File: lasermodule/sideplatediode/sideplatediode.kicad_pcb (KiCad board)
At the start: 2 copper layers, 117 x 33.2 mm, 4 parts, among them J1 Conn_01x02

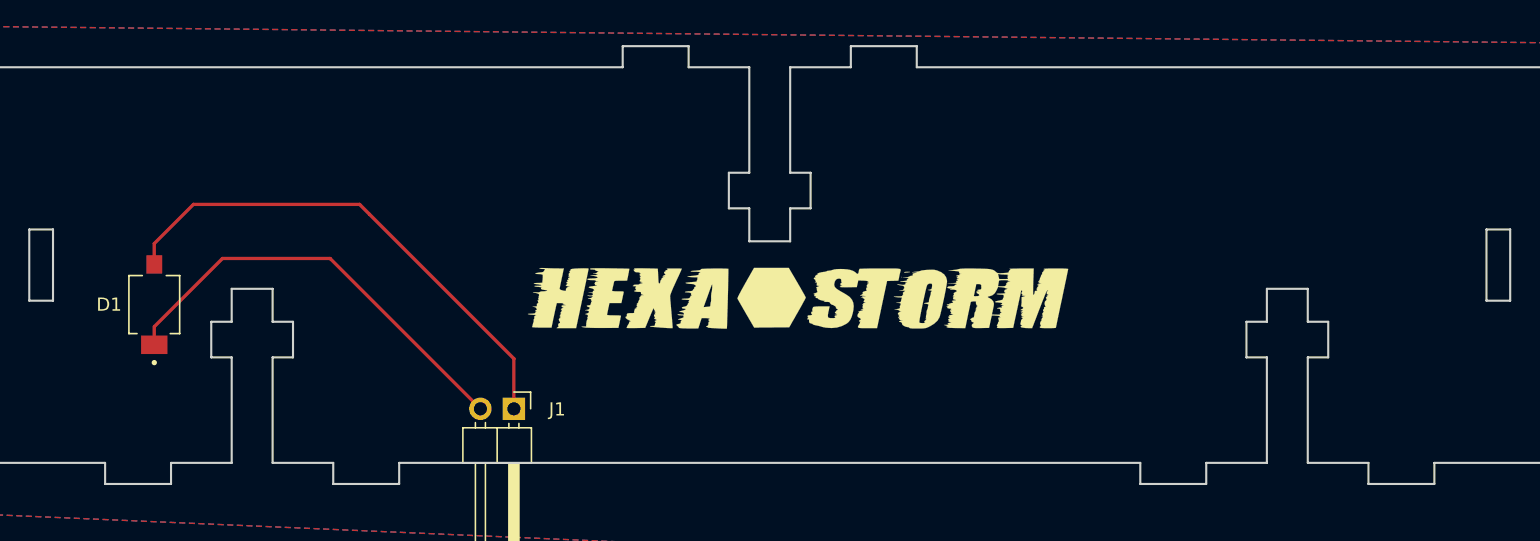
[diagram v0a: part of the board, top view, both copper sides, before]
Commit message: removed need for screws using pcb pads
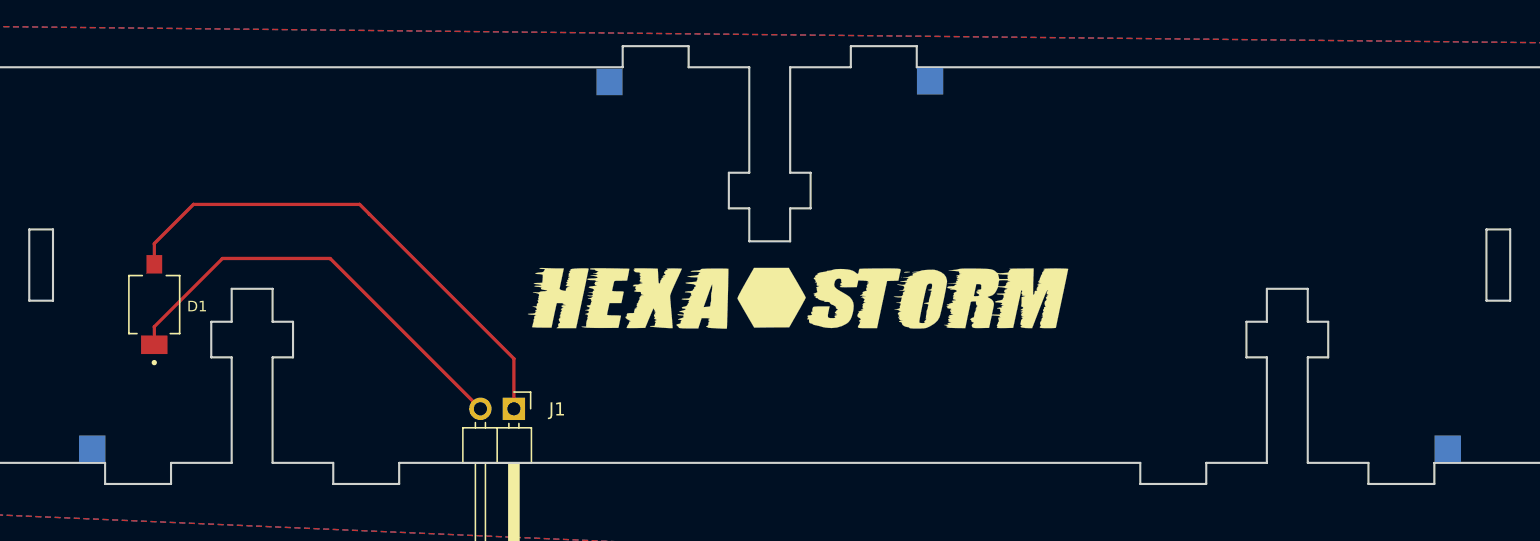
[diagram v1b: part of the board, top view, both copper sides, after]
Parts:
- added J2: Conn_01x01, start-of-scanline-detector:TestPoint_Pad_2.0x2.0mm_nosilk, B.Cu at (50.1, 56.5)
- added J3: Conn_01x01, start-of-scanline-detector:TestPoint_Pad_2.0x2.0mm_nosilk, B.Cu at (74.4, 56.4)
- added J4: Conn_01x01, start-of-scanline-detector:TestPoint_Pad_2.0x2.0mm_nosilk, B.Cu at (113.6, 84.3)
- added J5: Conn_01x01, start-of-scanline-detector:TestPoint_Pad_2.0x2.0mm_nosilk, B.Cu at (10.9, 84.3)
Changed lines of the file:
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@@
   (net 1 "Net-(J1-Pin_1)")
   (net 2 "Net-(J1-Pin_2)")
+  (net 3 "unconnected-(J2-Pin_1-Pad1)")
+  (net 4 "unconnected-(J3-Pin_1-Pad1)")
+  (net 5 "unconnected-(J4-Pin_1-Pad1)")
+  (net 6 "unconnected-(J5-Pin_1-Pad1)")
   (footprint "start-of-scanline-detector:DIO_BPW_34_S-Z" (layer "F.Cu")
     (at 15.56 73.3555 -90)
@@
     (property "Sheetname" "")
     (attr smd)
-    (fp_text reference "D1" (at 0.0025 3.43) (layer "F.SilkS")
-        (effects (font (size 1 1) (thickness 0.15)))
+    (fp_text reference "D1" (at 0.1425 -3.25) (layer "F.SilkS")
+        (effects (font (size 0.8 0.8) (thickness 0.15)))
     )
-    (fp_text value "BPW_34_S-Z" (at 1.5896 2.6936 90) (layer "F.Fab")
+    (fp_text value "BPW_34_S-Z" (at 1.5896 2.6936 -90) (layer "F.Fab")
         (effects (font (size 0.64 0.64) (thickness 0.15)))
     )
@@
       (stroke (width 0.01) (type solid)) (fill solid) (layer "F.SilkS"))
   )
+  (footprint "start-of-scanline-detector:TestPoint_Pad_2.0x2.0mm_nosilk" (layer "B.Cu")
+    (at 50.08 56.478 180)
+    (descr "SMD rectangular pad as test Point, square 2.0mm side length")
+    (tags "test point SMD pad rectangle square")
+    (property "Sheetfile" "sideplatediode.kicad_sch")
+    (property "Sheetname" "")
+    (property "ki_description" "Generic connector, single row, 01x01, script generated (kicad-library-utils/schlib/autogen/connector/)")
+    (property "ki_keywords" "connector")
+    (attr exclude_from_pos_files)
+    (fp_text reference "J2" (at 0 1.998) (layer "B.SilkS") hide
+        (effects (font (size 1 1) (thickness 0.15)) (justify mirror))
+    )
+    (fp_text value "Conn_01x01" (at 0 -2.05) (layer "B.Fab")
+        (effects (font (size 1 1) (thickness 0.15)) (justify mirror))
+    )
+    (fp_text user "${REFERENCE}" (at 0 2) (layer "B.Fab")
+        (effects (font (size 1 1) (thickness 0.15)) (justify mirror))
+    )
+    (fp_line (start -1.5 1.5) (end -1.5 -1.5)
+      (stroke (width 0.05) (type solid)) (layer "B.CrtYd"))
+    (fp_line (start -1.5 1.5) (end 1.5 1.5)
+      (stroke (width 0.05) (type solid)) (layer "B.CrtYd"))
+    (fp_line (start 1.5 -1.5) (end -1.5 -1.5)
+      (stroke (width 0.05) (type solid)) (layer "B.CrtYd"))
+    (fp_line (start 1.5 -1.5) (end 1.5 1.5)
+      (stroke (width 0.05) (type solid)) (layer "B.CrtYd"))
+    (pad "1" smd rect (at 0 0 180) (size 2 2) (layers "B.Cu" "B.Mask")
+      (net 3 "unconnected-(J2-Pin_1-Pad1)") (pinfunction "Pin_1") (pintype "passive+no_connect"))
+  )
+  (footprint "start-of-scanline-detector:TestPoint_Pad_2.0x2.0mm_nosilk" (layer "B.Cu")
+    (at 10.86 84.278 180)
+    (descr "SMD rectangular pad as test Point, square 2.0mm side length")
+    (tags "test point SMD pad rectangle square")
+    (property "Sheetfile" "sideplatediode.kicad_sch")
+    (property "Sheetname" "")
+    (property "ki_description" "Generic connector, single row, 01x01, script generated (kicad-library-utils/schlib/autogen/connector/)")
+    (property "ki_keywords" "connector")
+    (attr exclude_from_pos_files)
+    (fp_text reference "J5" (at 0 1.998) (layer "B.SilkS") hide
+        (effects (font (size 1 1) (thickness 0.15)) (justify mirror))
+    )
+    (fp_text value "Conn_01x01" (at 0 -2.05) (layer "B.Fab")
+        (effects (font (size 1 1) (thickness 0.15)) (justify mirror))
+    )
+    (fp_text user "${REFERENCE}" (at 0 2) (layer "B.Fab")
+        (effects (font (size 1 1) (thickness 0.15)) (justify mirror))
+    )
+    (fp_line (start -1.5 1.5) (end -1.5 -1.5)
+      (stroke (width 0.05) (type solid)) (layer "B.CrtYd"))
+    (fp_line (start -1.5 1.5) (end 1.5 1.5)
+      (stroke (width 0.05) (type solid)) (layer "B.CrtYd"))
+    (fp_line (start 1.5 -1.5) (end -1.5 -1.5)
+      (stroke (width 0.05) (type solid)) (layer "B.CrtYd"))
+    (fp_line (start 1.5 -1.5) (end 1.5 1.5)
+      (stroke (width 0.05) (type solid)) (layer "B.CrtYd"))
+    (pad "1" smd rect (at 0 0 180) (size 2 2) (layers "B.Cu" "B.Mask")
+      (net 6 "unconnected-(J5-Pin_1-Pad1)") (pinfunction "Pin_1") (pintype "passive+no_connect"))
+  )
+  (footprint "start-of-scanline-detector:TestPoint_Pad_2.0x2.0mm_nosilk" (layer "B.Cu")
+    (at 113.64 84.278 180)
+    (descr "SMD rectangular pad as test Point, square 2.0mm side length")
+    (tags "test point SMD pad rectangle square")
+    (property "Sheetfile" "sideplatediode.kicad_sch")
+    (property "Sheetname" "")
+    (property "ki_description" "Generic connector, single row, 01x01, script generated (kicad-library-utils/schlib/autogen/connector/)")
+    (property "ki_keywords" "connector")
+    (attr exclude_from_pos_files)
+    (fp_text reference "J4" (at 0 1.998) (layer "B.SilkS") hide
+        (effects (font (size 1 1) (thickness 0.15)) (justify mirror))
+    )
+    (fp_text value "Conn_01x01" (at 0 -2.05) (layer "B.Fab")
+        (effects (font (size 1 1) (thickness 0.15)) (justify mirror))
+    )
+    (fp_text user "${REFERENCE}" (at 0 2) (layer "B.Fab")
+        (effects (font (size 1 1) (thickness 0.15)) (justify mirror))
+    )
+    (fp_line (start -1.5 1.5) (end -1.5 -1.5)
+      (stroke (width 0.05) (type solid)) (layer "B.CrtYd"))
+    (fp_line (start -1.5 1.5) (end 1.5 1.5)
+      (stroke (width 0.05) (type solid)) (layer "B.CrtYd"))
+    (fp_line (start 1.5 -1.5) (end -1.5 -1.5)
+      (stroke (width 0.05) (type solid)) (layer "B.CrtYd"))
+    (fp_line (start 1.5 -1.5) (end 1.5 1.5)
+      (stroke (width 0.05) (type solid)) (layer "B.CrtYd"))
+    (pad "1" smd rect (at 0 0 180) (size 2 2) (layers "B.Cu" "B.Mask")
+      (net 5 "unconnected-(J4-Pin_1-Pad1)") (pinfunction "Pin_1") (pintype "passive+no_connect"))
+  )
   (footprint "start-of-scanline-detector:hexastorm" (layer "B.Cu")
     (at 60.43 72.858 180)
@@
       (stroke (width 0.01) (type solid)) (fill solid) (layer "B.SilkS"))
   )
+  (footprint "start-of-scanline-detector:TestPoint_Pad_2.0x2.0mm_nosilk" (layer "B.Cu")
+    (at 74.39 56.428 180)
+    (descr "SMD rectangular pad as test Point, square 2.0mm side length")
+    (tags "test point SMD pad rectangle square")
+    (property "Sheetfile" "sideplatediode.kicad_sch")
+    (property "Sheetname" "")
+    (property "ki_description" "Generic connector, single row, 01x01, script generated (kicad-library-utils/schlib/autogen/connector/)")
+    (property "ki_keywords" "connector")
+    (attr exclude_from_pos_files)
+    (fp_text reference "J3" (at 0 1.998) (layer "B.SilkS") hide
+        (effects (font (size 1 1) (thickness 0.15)) (justify mirror))
+    )
+    (fp_text value "Conn_01x01" (at 0 -2.05) (layer "B.Fab")
+        (effects (font (size 1 1) (thickness 0.15)) (justify mirror))
+    )
+    (fp_text user "${REFERENCE}" (at 0 2) (layer "B.Fab")
+        (effects (font (size 1 1) (thickness 0.15)) (justify mirror))
+    )
+    (fp_line (start -1.5 1.5) (end -1.5 -1.5)
+      (stroke (width 0.05) (type solid)) (layer "B.CrtYd"))
+    (fp_line (start -1.5 1.5) (end 1.5 1.5)
+      (stroke (width 0.05) (type solid)) (layer "B.CrtYd"))
+    (fp_line (start 1.5 -1.5) (end -1.5 -1.5)
+      (stroke (width 0.05) (type solid)) (layer "B.CrtYd"))
+    (fp_line (start 1.5 -1.5) (end 1.5 1.5)
+      (stroke (width 0.05) (type solid)) (layer "B.CrtYd"))
+    (pad "1" smd rect (at 0 0 180) (size 2 2) (layers "B.Cu" "B.Mask")
+      (net 4 "unconnected-(J3-Pin_1-Pad1)") (pinfunction "Pin_1") (pintype "passive+no_connect"))
+  )
   (gr_line (start 99.93 77.358) (end 98.38 77.358)

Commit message: board almost fully synced close for release
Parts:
- removed J1: Conn_01x02, Connector_PinHeader_2.54mm:PinHeader_1x02_P2.54mm_Horizontal
- J2, J3, J4, J5, L1: moved to F.Cu
- L2: moved to B.Cu
- moved J5 100.1 mm to (107.2, 111.5), turned to 0 degrees
- moved J2 98.4 mm to (142.4, 90.5), turned to 0 degrees
- moved D1 97.0 mm to (109.2, 98.5)
- moved L1 96.8 mm to (153.0, 101.0), turned to 0 degrees
- moved J3 91.9 mm to (159.7, 90.5), turned to 0 degrees
- moved L2 89.3 mm to (149.1, 101.0), turned to 180 degrees
- moved J4 85.6 mm to (194.8, 111.5), turned to 0 degrees
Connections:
- D1 pad A: Net-(J1-Pin_1) -> GND
- D1 pad C: Net-(J1-Pin_2) -> DiodeK
- J4 pad 1: unconnected-(J4-Pin_1-Pad1) -> GND
- J5 pad 1: unconnected-(J5-Pin_1-Pad1) -> DiodeK
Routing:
- net Net-(J1-Pin_1): track 38.7 -> 0.00 mm
- net Net-(J1-Pin_2): track 33.0 -> 0.00 mm
- net DiodeK: track 0.00 -> 11.7 mm, vias 0 -> 1
- net GND: vias 0 -> 1
- added copper zone on B.Cu, net GND
- added copper zone on F.Cu, net GND
- removed copper zone on B.Cu, net Net-(J1-Pin_1)
- removed copper zone on F.Cu, net Net-(J1-Pin_1)
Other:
- board size 117 x 33.2 mm -> 108.7 x 24.2 mm
- board text added: "pos 2"
- board text added: "pos1"

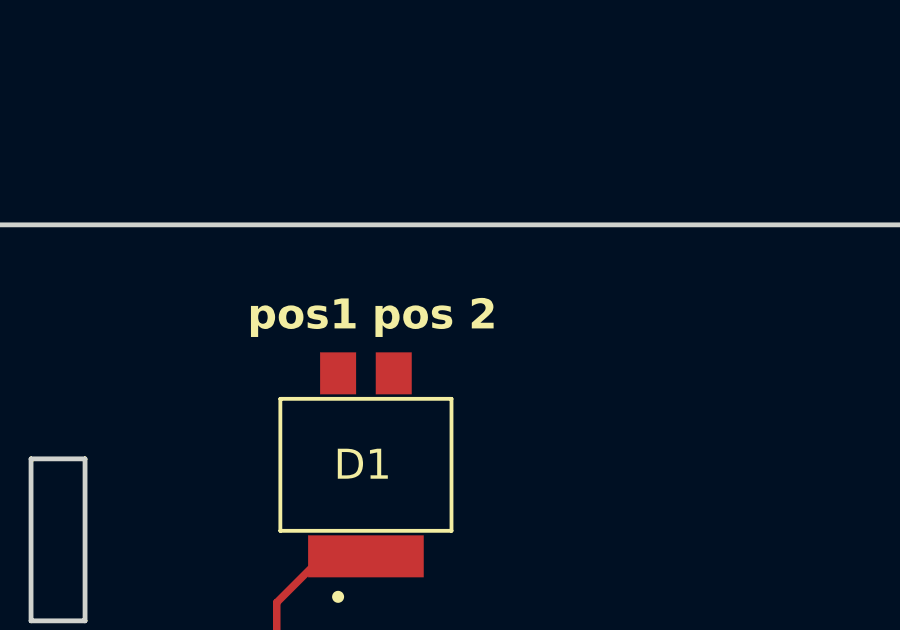
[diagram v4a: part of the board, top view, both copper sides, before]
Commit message: fixed typo, added standoff lasermodule
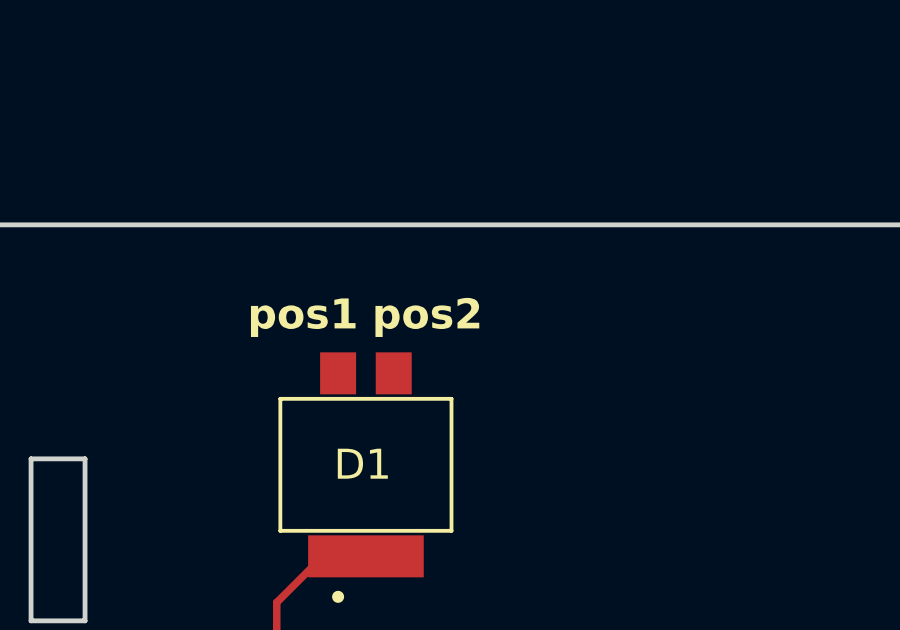
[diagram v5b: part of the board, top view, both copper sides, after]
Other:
- board text added: "pos2"
- board text removed: "pos 2"
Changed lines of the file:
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@@
 		(layer "Edge.Cuts")
 	)
-	(gr_text "pos 2\n"
+	(gr_text "pos2\n"
 		(at 110.375 94.075 0)
 		(layer "F.SilkS")

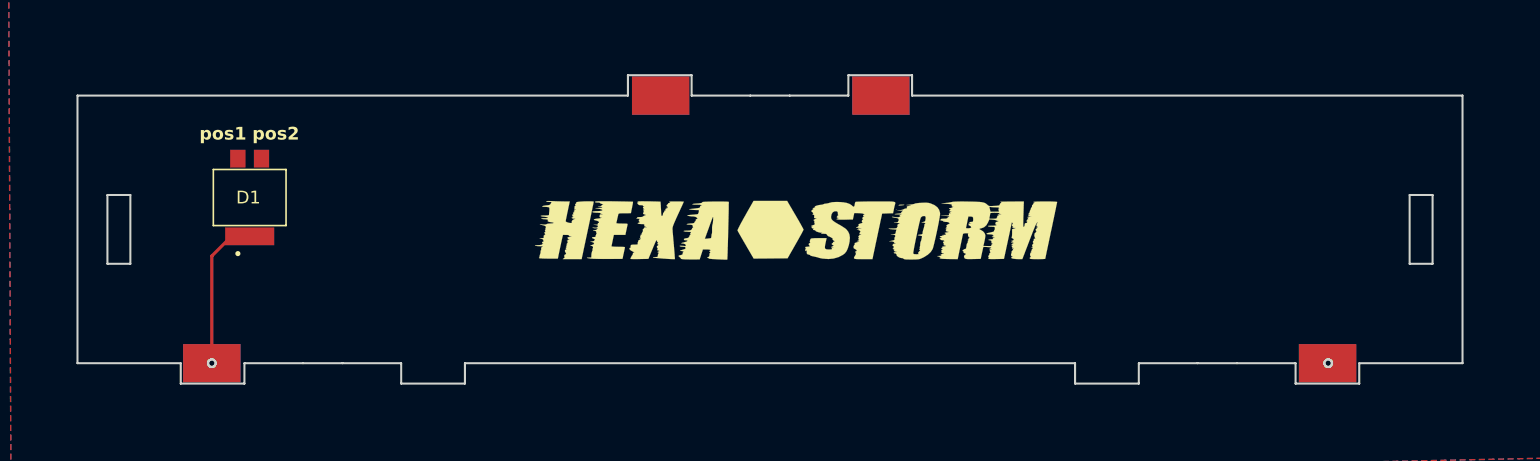
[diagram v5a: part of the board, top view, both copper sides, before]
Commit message: changes to reduce prices pcbway
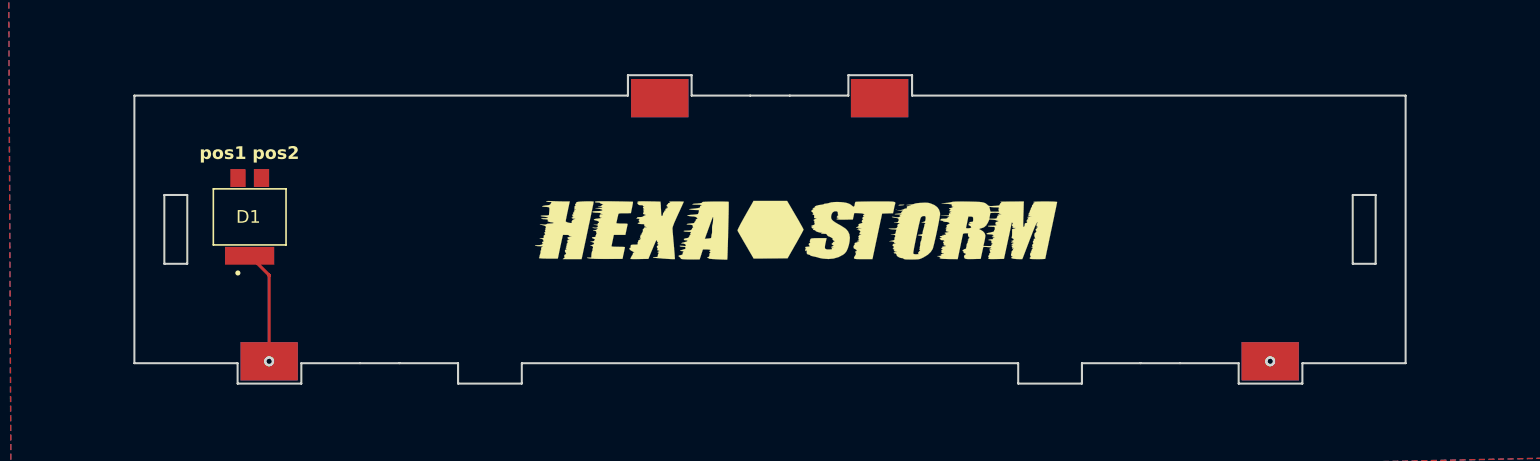
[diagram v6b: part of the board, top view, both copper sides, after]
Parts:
- moved J4 4.50 mm to (190.2, 111.3)
- moved J5 4.50 mm to (111.7, 111.3)
- moved D1 1.52 mm to (109.2, 100.0)
- moved J3 0.22 mm to (159.6, 90.7)
- moved J2 0.21 mm to (142.3, 90.7)
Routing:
- net DiodeK: track 11.7 -> 8.91 mm
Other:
- board size 108.7 x 24.2 mm -> 99.8 x 24.2 mm
